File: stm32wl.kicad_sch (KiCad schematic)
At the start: 1 part, among them U201 STM32WLE5CCUx

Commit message: STM power mostly done
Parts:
- added C309 (x5): 4.7u, Capacitor_SMD:C_0603_1608Metric, symbol Device:C
- added C309 (x11): 100n, Capacitor_SMD:C_0402_1005Metric, symbol Device:C
- added C309 (x3): 33p, Capacitor_SMD:C_0402_1005Metric, symbol Device:C
- added C309: 3.3p, Capacitor_SMD:C_0402_1005Metric, symbol Device:C
- added C309: 470n, Capacitor_SMD:C_0603_1608Metric, symbol Device:C
- added L201: 15u, symbol Device:L
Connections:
- net VDD: now reaches U201.11 (VDD)
- net VDD: now also U201.28 (VDDRF), U201.41 (VDDA), U201.44 (VDD), U201.46 (VDDSMPS), C309.1, C309.1, C309.1, C309.1, C309.1, C309.1, C309.1, C309.1, C309.1, C309.1, C309.1, C309.1, C309.1
- net RFI_N: now reaches U201.20 (RFI_P)
- net RFI_N: now also U201.21 (RFI_N)
- net RFO_LP: now reaches U201.22 (RFO_LP)
- net VR_PA: now reaches U201.24 (VR_PA)
- net VDDPA: now reaches U201.25 (VDDPA)
- net VDDPA: now also U201.29 (VDDRF1V55), U201.45 (VFBSMPS), C309.1, C309.1, C309.1, C309.1, C309.1, C309.1, L201.2
- net VBAT: now reaches U201.37 (VBAT)
- net VBAT: now also C309.1, C309.1
- net VLXMPS: now reaches U201.47 (VLXSMPS)
- net GND: now reaches U201.48 (VSSSMPS)
- net GND: now also U201.49 (VSS), C309.2, C309.2, C309.2, C309.2, C309.2, C309.2, C309.2, C309.2, C309.2, C309.2, C309.2, C309.2, C309.2, C309.2, C309.2, C309.2, C309.2, C309.2, C309.2, C309.2, C309.2
- new net VLXSMPS: L201.1
- no-connect marks 0 -> 1
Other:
- moved on the sheet: U201

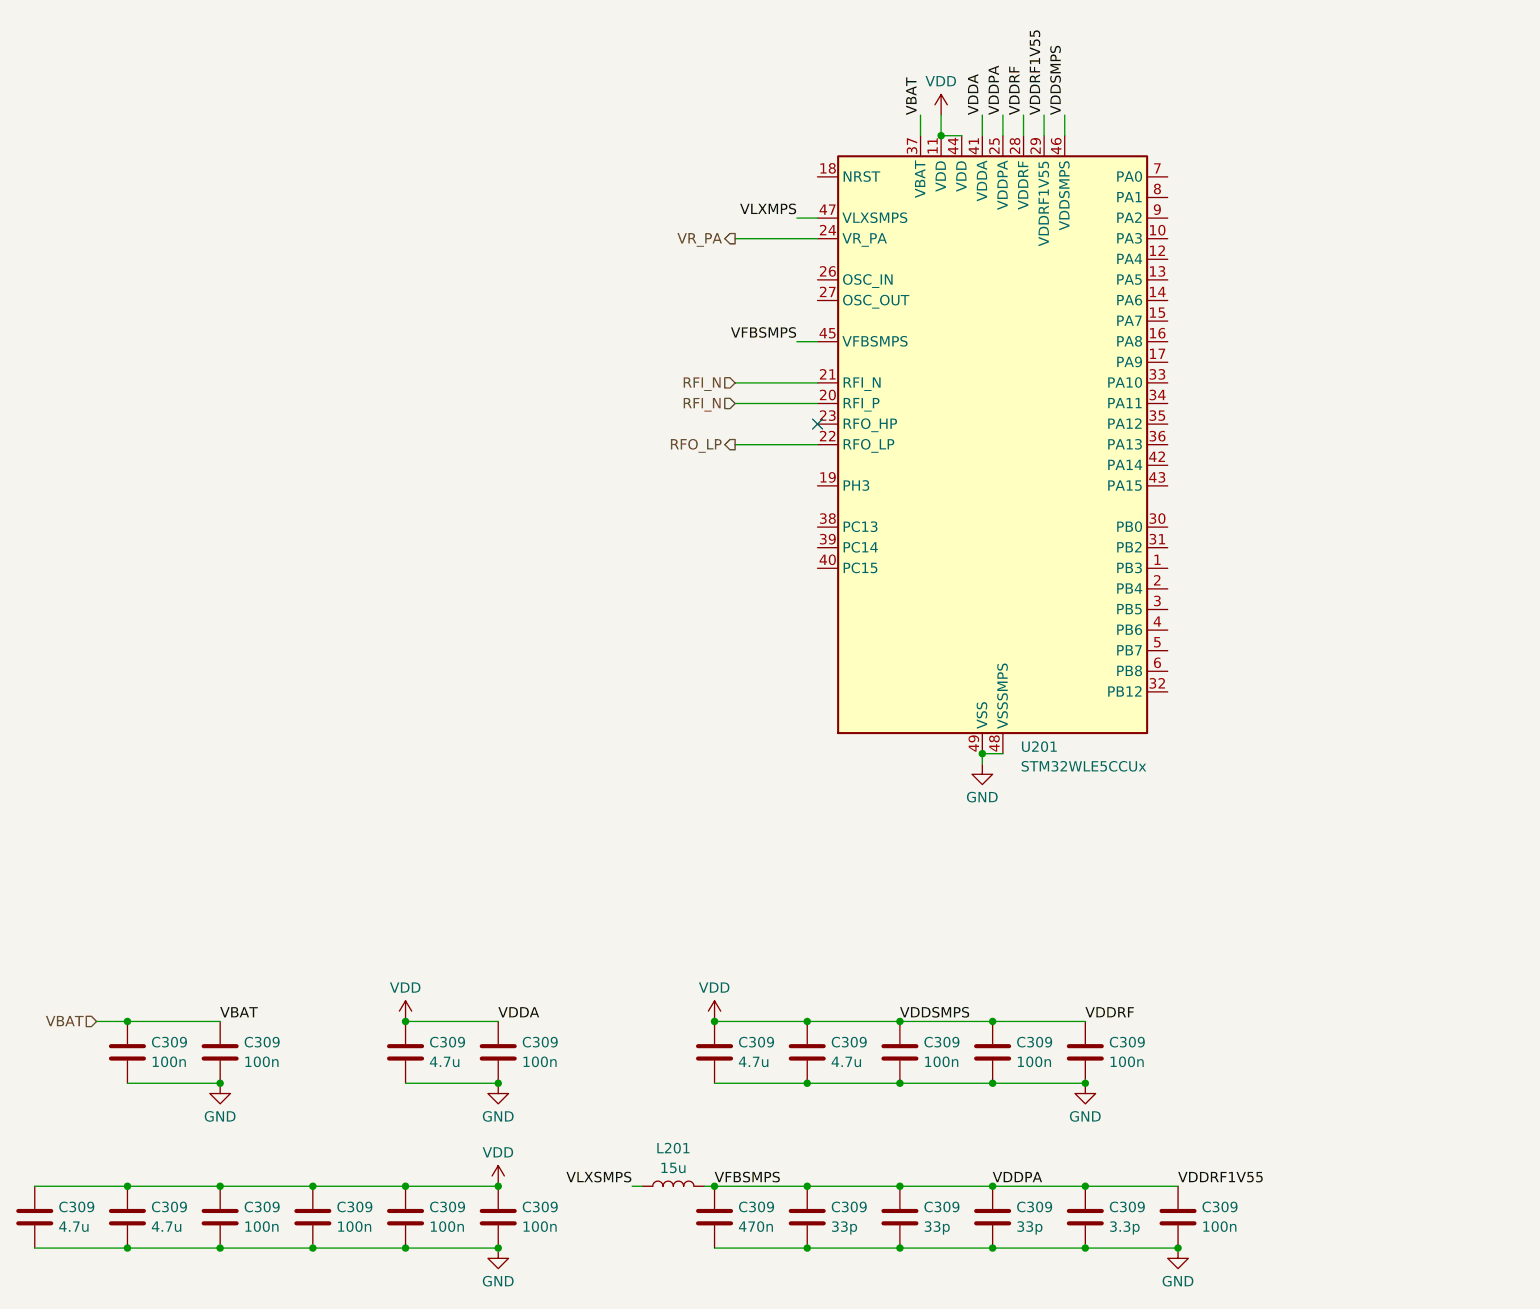
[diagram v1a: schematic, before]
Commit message: added cubemx file for checking pinout
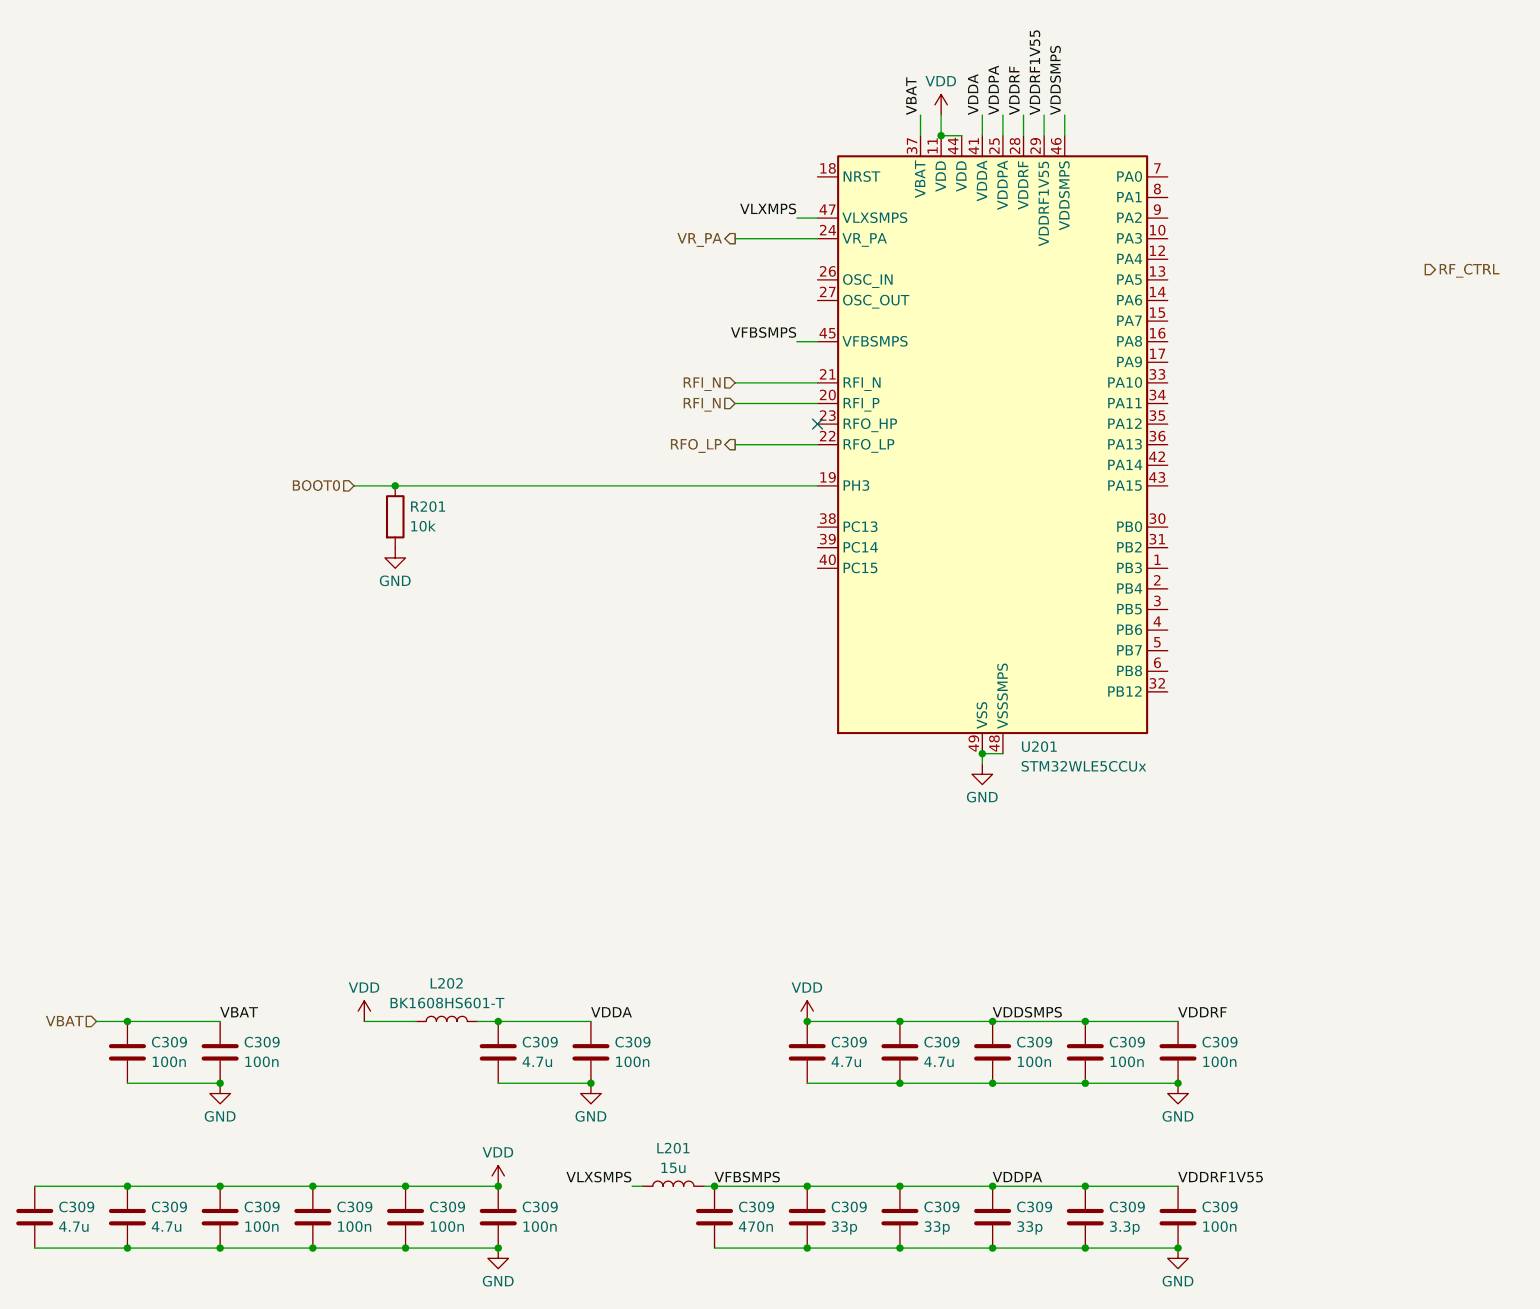
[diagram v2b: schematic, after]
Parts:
- added L202: BK1608HS601-T, Inductor_SMD:L_0603_1608Metric, symbol Device:L
- added R201: 10k, Resistor_SMD:R_0402_1005Metric, symbol Device:R
- L201: footprint (none) -> Inductor_SMD:L_0805_2012Metric
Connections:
- net GND: now also R201.2
- net VDD: now also L202.1; no longer C309.1, C309.1, U201.41 (VDDA)
- net BOOT0: now reaches U201.19 (PH3)
- net BOOT0: now also R201.1
- new net VDDA: C309.1, C309.1, L202.2, U201.41 (VDDA)
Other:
- moved on the sheet: C309

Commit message: most components placed, routed the RF section
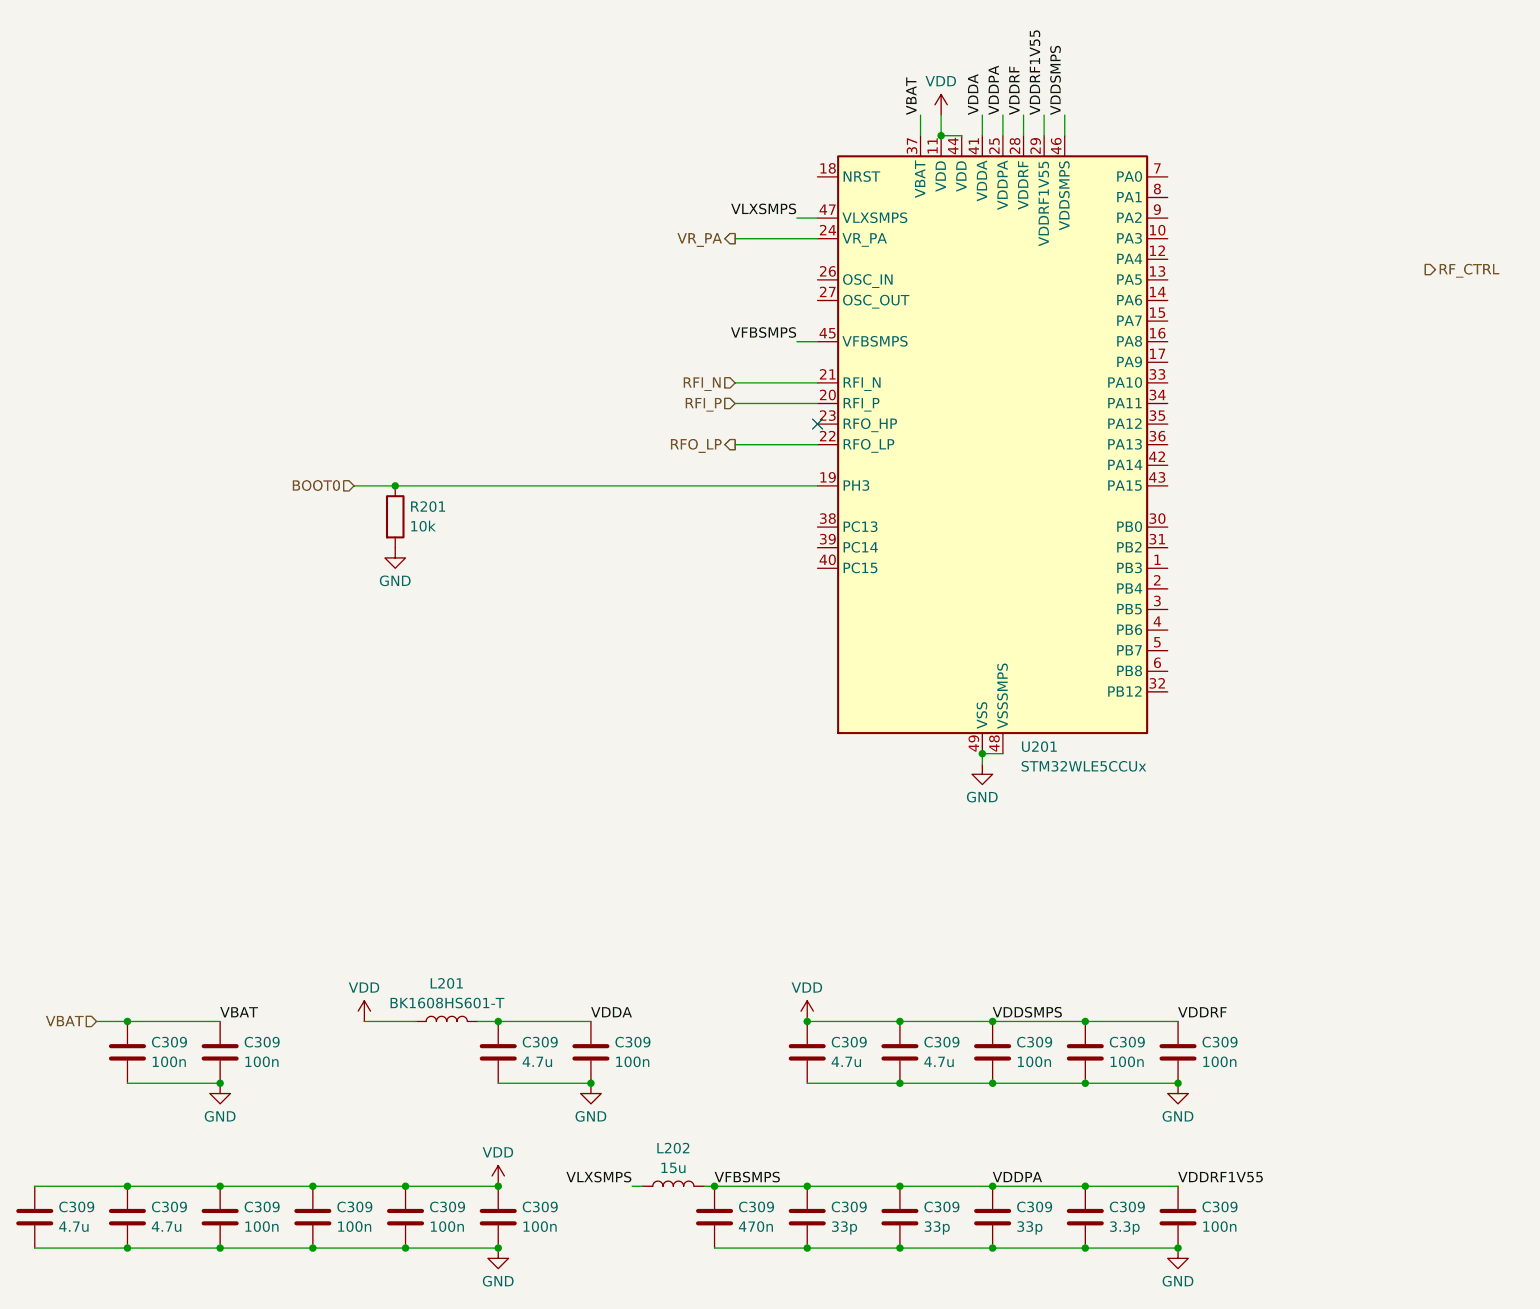
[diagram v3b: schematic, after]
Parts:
- renumbered L202 to L201, L201 to L202
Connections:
- net VLXMPS is gone; now on net VLXSMPS: U201.47 (VLXSMPS)
- net RFI_N: no longer U201.20 (RFI_P)
- new net RFI_P: U201.20 (RFI_P)

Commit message: most of the components are placed
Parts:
- removed C309: 4.7u, Capacitor_SMD:C_0603_1608Metric, symbol Device:C
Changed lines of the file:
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@@
   (junction (at 53.34 181.61) (diameter 0) (color 0 0 0 0)
   )
-  (junction (at 30.48 181.61) (diameter 0) (color 0 0 0 0)
-  )
   (junction (at 64.77 189.23) (diameter 0) (color 0 0 0 0)
   )
@@
   )
   (junction (at 148.59 181.61) (diameter 0) (color 0 0 0 0)
-  )
-  (junction (at 30.48 189.23) (diameter 0) (color 0 0 0 0)
   )
   (junction (at 76.2 181.61) (diameter 0) (color 0 0 0 0)
@@
     (stroke (width 0) (type default))
   )
-  (wire (pts (xy 19.05 181.61) (xy 30.48 181.61))
-    (stroke (width 0) (type default))
-  )
   (wire (pts (xy 148.59 161.29) (xy 137.16 161.29))
     (stroke (width 0) (type default))
@@
   )
   (wire (pts (xy 138.43 49.53) (xy 138.43 52.07))
-    (stroke (width 0) (type default))
-  )
-  (wire (pts (xy 19.05 189.23) (xy 30.48 189.23))
     (stroke (width 0) (type default))
   )
@@
         )
       )
-    )
-  )
-  (symbol (lib_id "Device:C") (at 19.05 185.42 0) (unit 1)
-    (in_bom yes) (on_board yes) (dnp no) (fields_autoplaced)
-    (property "Reference" "C309" (at 21.971 184.2079 0)
-      (effects (font (size 1.27 1.27)) (justify left))
-    )
-    (property "Value" "4.7u" (at 21.971 186.6321 0)
-      (effects (font (size 1.27 1.27)) (justify left))
-    )
-    (property "Footprint" "Capacitor_SMD:C_0603_1608Metric" (at 20.0152 189.23 0)
-      (effects (font (size 1.27 1.27)) hide)
-    )
-    (property "Datasheet" "~" (at 19.05 185.42 0)
-      (effects (font (size 1.27 1.27)) hide)
-    )
-    (pin "1")
-    (pin "2")
-    (instances
-      (project "lora-module"
-        (path "/30c7e509-35af-4828-996b-9681d057624f/8ccb3257-dd21-406f-b73b-aadedfaf4fa0"
-          (reference "C309") (unit 1)
-        )
-        (path "/30c7e509-35af-4828-996b-9681d057624f/93ed2c4d-2004-4e0b-a952-c18d2f9b026d"
-          (reference "C201") (unit 1)
-        )
-      )
